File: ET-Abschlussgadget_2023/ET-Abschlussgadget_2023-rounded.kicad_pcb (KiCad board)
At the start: 2 copper layers, 85 x 54 mm, 35 parts, among them J1 PB0, J2 PB1, J3 UPDI / RESET, J4 EXTCLK, J5 EXTCLK, J6 EXTCLK, SW1 ON/OFF, U1 ATtiny414-SS

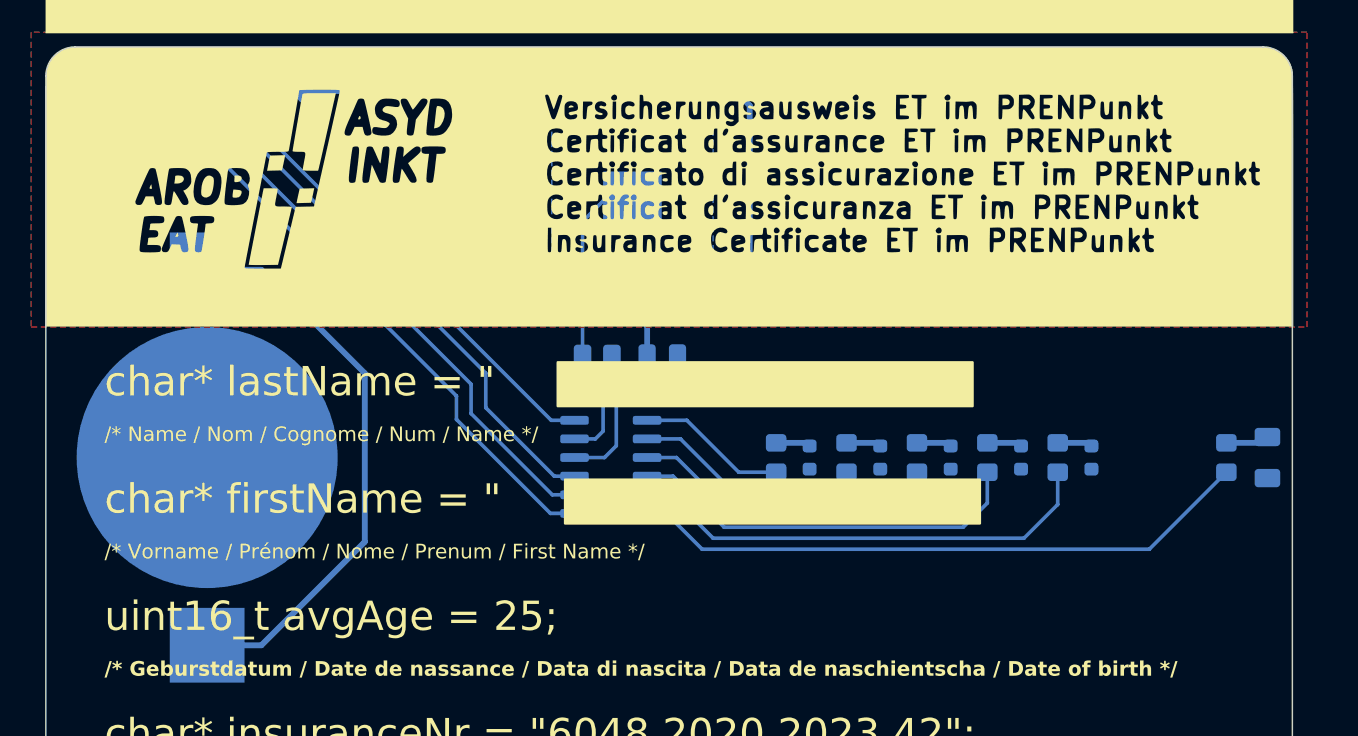
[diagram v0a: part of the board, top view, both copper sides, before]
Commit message: Redone whole layout based around new MCU, button and batteryholder-footprints are still placeholder tbd
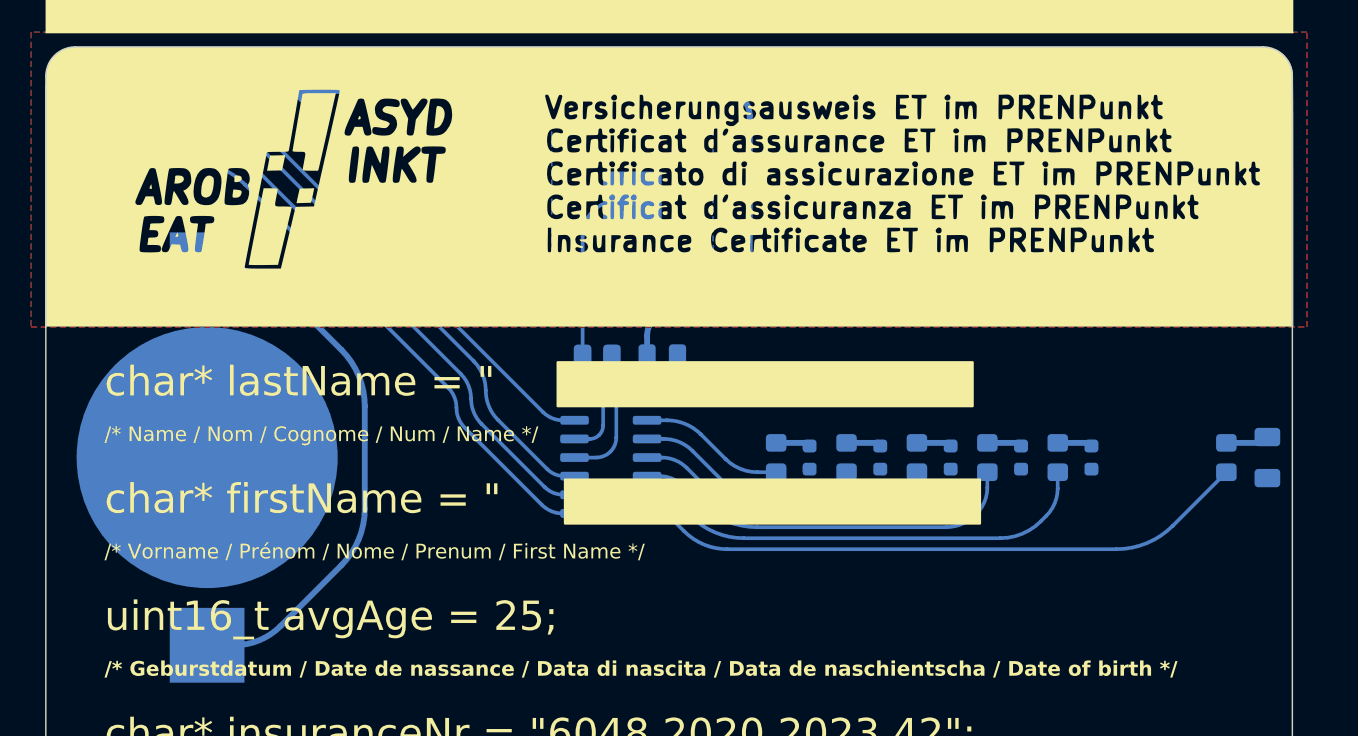
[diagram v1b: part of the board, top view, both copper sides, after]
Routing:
- net Net-(BT1-+): track 38.8 -> 37.9 mm
- net Net-(J2-Pin_1): track 47.0 -> 46.2 mm
- net Net-(J1-Pin_1): track 44.8 -> 44.0 mm
- net /LED 1: track 32.4 -> 31.7 mm
- net VCC: track 56.0 -> 55.3 mm
- net /LED 2: track 27.4 -> 26.8 mm
- net /LED 3: track 22.2 -> 21.6 mm
- net /UPDI / RESET: track 39.3 -> 38.8 mm
- net /LED 4: track 17.1 -> 16.6 mm
- net /LED IR: track 42.7 -> 42.1 mm

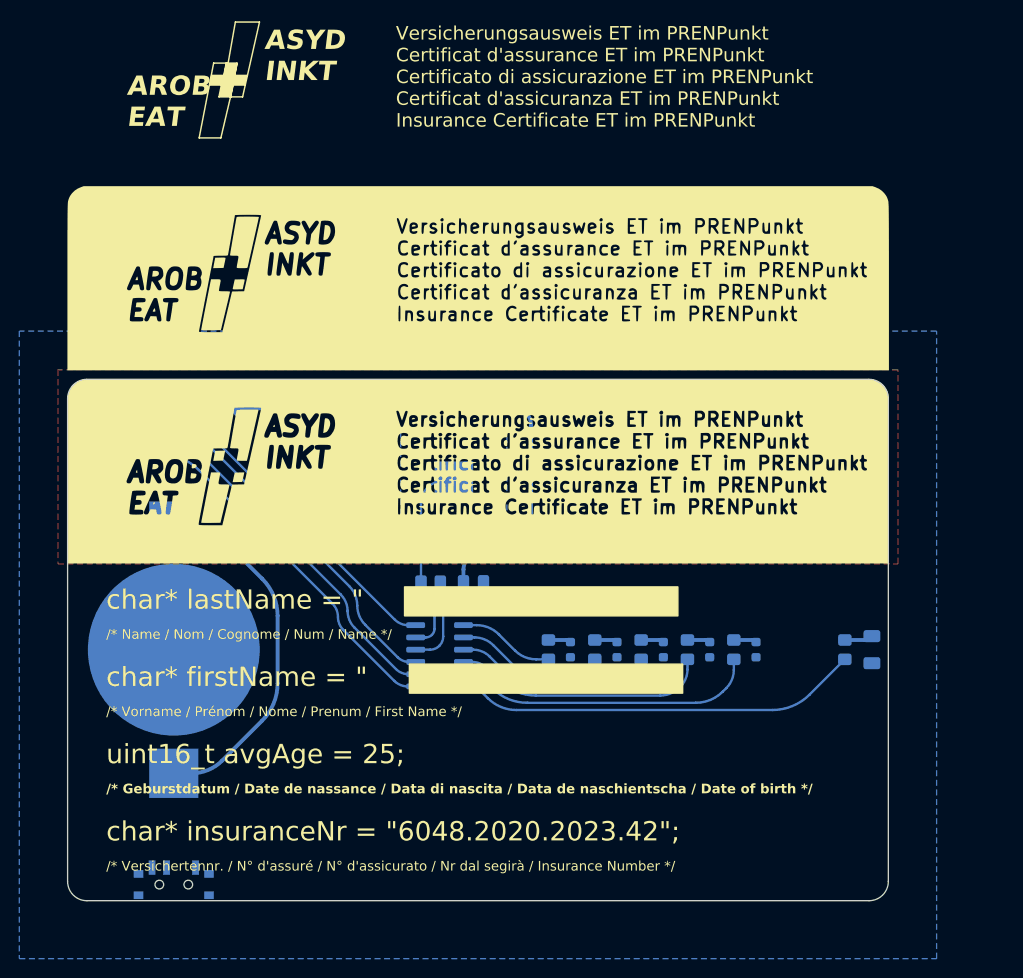
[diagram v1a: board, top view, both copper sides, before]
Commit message: Improve back silkscreen and routing
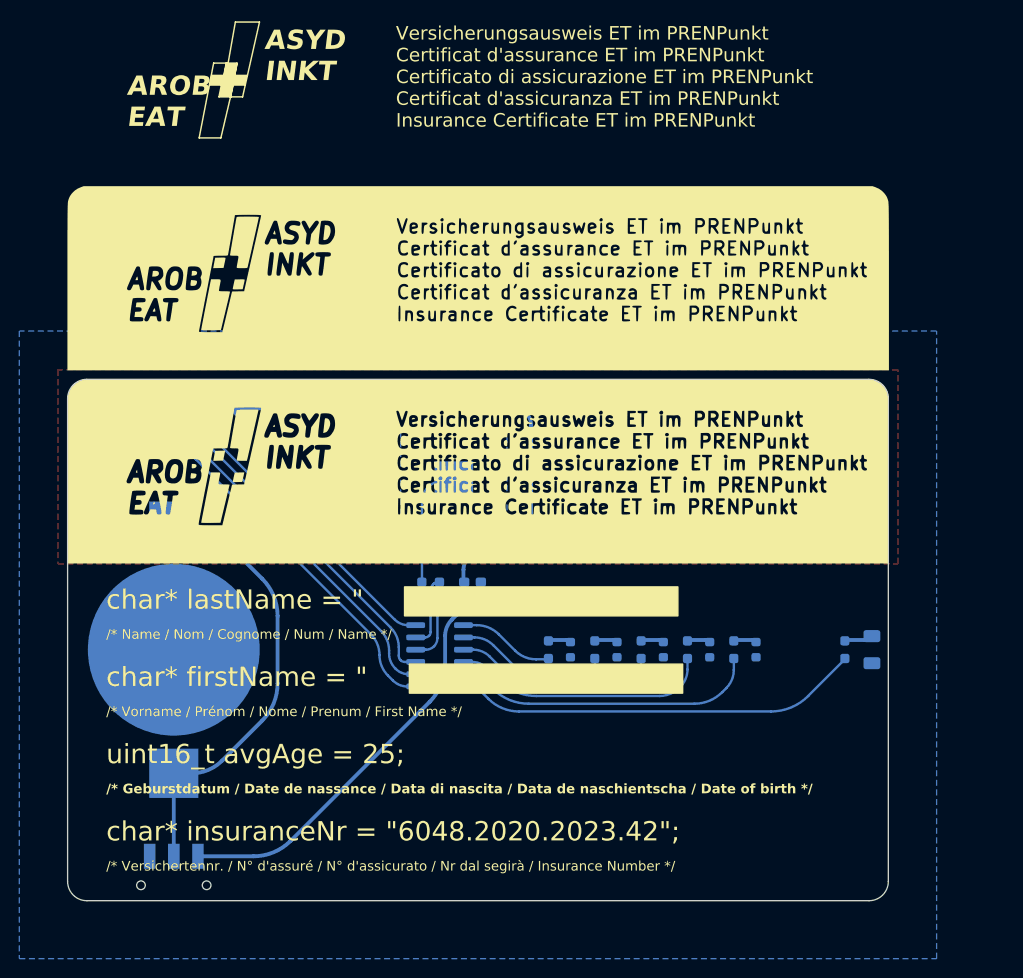
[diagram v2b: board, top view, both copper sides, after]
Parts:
- added kibuzzard-64480F6A: G***, kibuzzard-64480F6A, B.Cu at (128.7, 124.8)
- C1: footprint Capacitor_SMD:C_0805_2012Metric_Pad1.18x1.45mm_HandSolder -> Capacitor_SMD:C_0603_1608Metric_Pad1.08x0.95mm_HandSolder
- R1, R2, R3, R4, R5, R6, R7: footprint Resistor_SMD:R_0805_2012Metric_Pad1.20x1.40mm_HandSolder -> Resistor_SMD:R_0603_1608Metric_Pad0.98x0.95mm_HandSolder
- SW1: footprint Button_Switch_SMD:SW_SPDT_PCM12 -> Button_Switch_SMD:DEALON_MK-12D04-G2
- moved SW1 0.40 mm to (111.0, 132.4), turned to 0 degrees
- moved C1 0.10 mm to (141.9, 101.0)
- turned D1 to 90 degrees
- turned D2 to 90 degrees
- turned D3 to 90 degrees
- turned D4 to 90 degrees
- turned D5 to 90 degrees
- turned D6 to 90 degrees
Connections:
- D1 pad 1: Net-(D1-K) -> GND
- D1 pad 2: GND -> Net-(D1-A)
- D2 pad 1: Net-(D2-K) -> GND
- D2 pad 2: GND -> Net-(D2-A)
- D3 pad 1: Net-(D3-K) -> GND
- D3 pad 2: GND -> Net-(D3-A)
- D4 pad 1: Net-(D4-K) -> GND
- D4 pad 2: GND -> Net-(D4-A)
- D5 pad 1: Net-(D5-K) -> GND
- D5 pad 2: GND -> Net-(D5-A)
- D6 pad 1: Net-(D6-K) -> GND
- D6 pad 2: GND -> Net-(D6-A)
- R1 pad 1: Net-(D1-K) -> Net-(D1-A)
- R2 pad 1: Net-(D2-K) -> Net-(D2-A)
- R3 pad 2: Net-(D3-K) -> Net-(D3-A)
- R4 pad 2: Net-(D4-K) -> Net-(D4-A)
- R6 pad 1: Net-(D5-K) -> Net-(D5-A)
- R7 pad 1: Net-(D6-K) -> Net-(D6-A)
- SW1 pad 1: VCC -> unconnected-(SW1-A-Pad1)
- SW1 pad 3: unconnected-(SW1-C-Pad3) -> VCC
- U1 pad 12: /Cap_Pad -> /Cap_Pad / ADC1
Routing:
- net VCC: track 55.3 -> 96.1 mm
- net Net-(BT1-+): track 37.9 -> 47.1 mm
- net /Cap_Pad: track 20.5 -> 12.8 mm
- net /Cap_Pad / ADC1: track 9.35 -> 16.2 mm
- net Net-(D1-K): track 2.93 -> 0.00 mm
- net Net-(D1-A): track 0.00 -> 2.93 mm
- net Net-(D3-K): track 2.37 -> 0.00 mm
- net Net-(D3-A): track 0.00 -> 2.37 mm
- net Net-(D5-K): track 2.37 -> 0.00 mm
- net Net-(D5-A): track 0.00 -> 2.37 mm
- net Net-(D2-K): track 2.37 -> 0.00 mm
- net Net-(D2-A): track 0.00 -> 2.37 mm
- net Net-(D4-K): track 2.37 -> 0.00 mm
- net Net-(D4-A): track 0.00 -> 2.37 mm
- net Net-(D6-K): track 2.35 -> 0.00 mm
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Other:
- board text added: "ON"
- board text removed: "SCAN ME!"

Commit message: Move switch, Move testpads, Add spotify code
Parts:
- added G***: LOGO, LOGO, B.Cu at (127.5, 98.1)
- BT1: footprint Battery:BatteryHolder_Keystone_3002_1x2032 -> easyeda2kicad:BAT-SMD_CR2032-3V
- G*** (x2): value LOGO -> LOGO1
- SW1: footprint Button_Switch_SMD:DEALON_MK-12D04-G2 -> easyeda2kicad:SW-TH_MSK12C02
- moved SW1 8.86 mm to (103.9, 127.1), turned to 90 degrees
- moved J5 1.38 mm to (116.6, 83.0)
- moved J6 0.92 mm to (114.1, 83.0)
- moved J4 0.46 mm to (111.5, 83.0)
- moved J2 0.20 mm to (102.8, 83.0)
- turned BT1 to 180 degrees
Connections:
- SW1 pad 1: unconnected-(SW1-A-Pad1) -> VCC
- SW1 pad 3: VCC -> unconnected-(SW1-C-Pad3)
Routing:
- net VCC: track 96.1 -> 107.4 mm
- net Net-(BT1-+): track 47.1 -> 48.7 mm
- net /EXTCLK: track 33.3 -> 34.5 mm
- net Net-(J2-Pin_1): track 45.9 -> 46.9 mm
- net Net-(J1-Pin_1): track 43.5 -> 44.3 mm
- net /LED 1: track 31.8 -> 32.5 mm
- net /LED 2: track 26.8 -> 27.5 mm
- net /LED 3: track 21.6 -> 22.2 mm
- net /LED IR: track 42.3 -> 42.8 mm
- net /LED 4: track 16.6 -> 17.1 mm
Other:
- board text removed: "ET: {dblquote}Wie WI, nur besser{dblquote}"

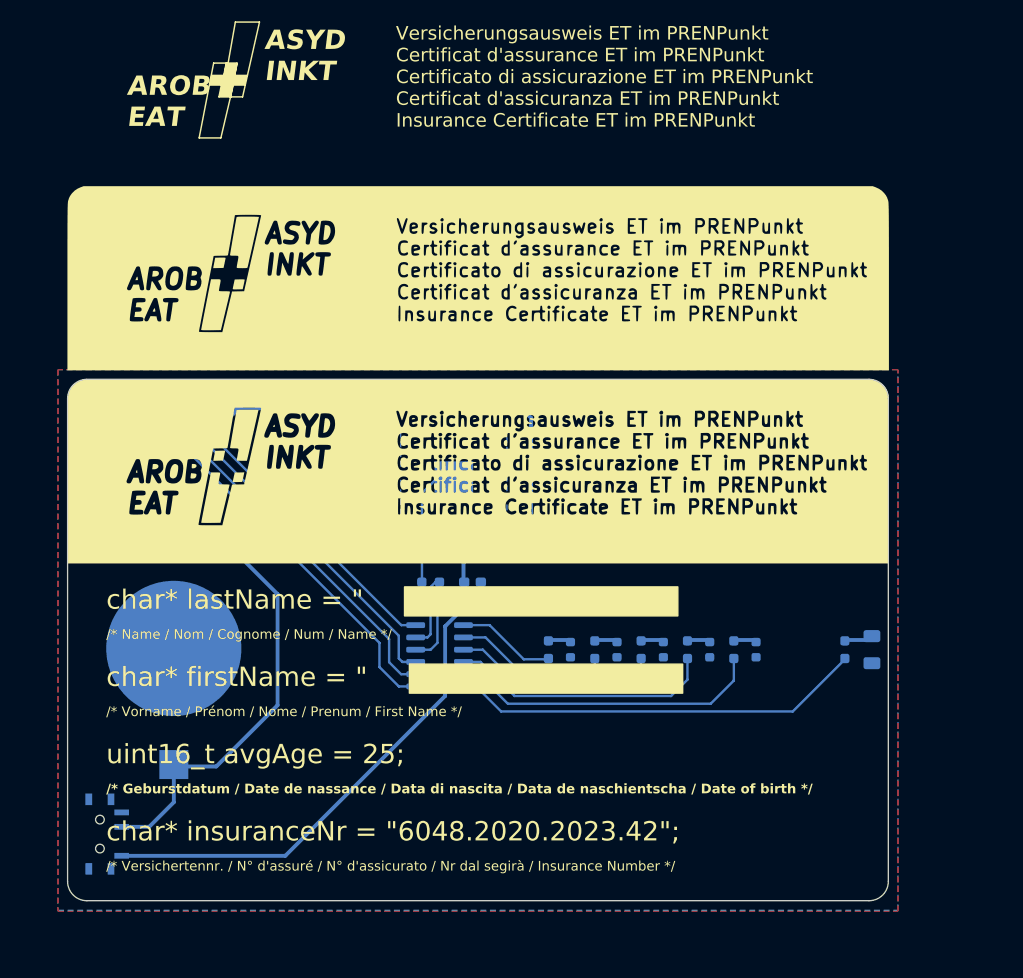
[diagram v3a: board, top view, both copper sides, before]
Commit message: Improve back copper pattern
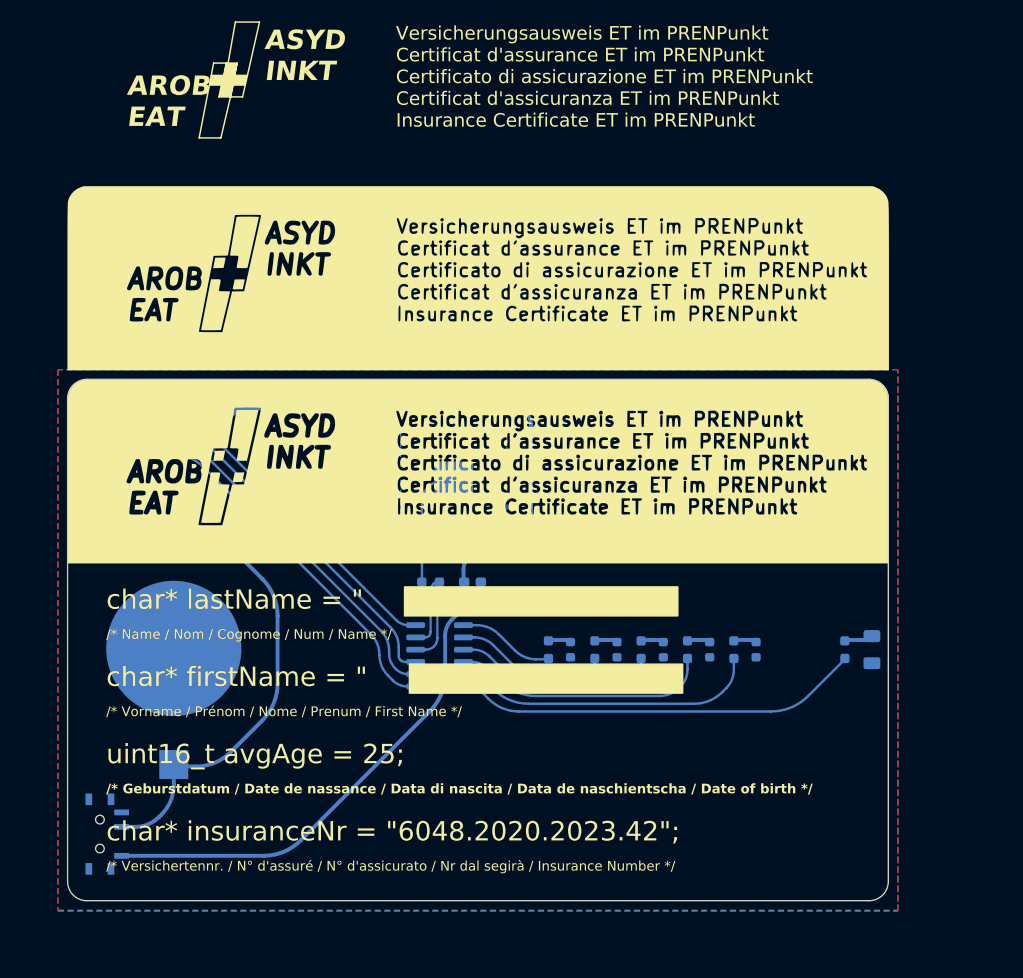
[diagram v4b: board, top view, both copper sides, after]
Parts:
- removed the G*** at (127.5, 98.1)
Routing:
- net Net-(BT1-+): track 48.7 -> 47.1 mm
- net VCC: track 107.4 -> 106.0 mm
- net Net-(J2-Pin_1): track 46.9 -> 46.0 mm
- net Net-(J1-Pin_1): track 44.3 -> 43.5 mm
- net /LED 1: track 32.5 -> 31.8 mm
- net /LED 2: track 27.5 -> 26.8 mm
- net /LED 3: track 22.2 -> 21.6 mm
- net /UPDI / RESET: track 40.0 -> 39.4 mm
- net /LED IR: track 42.8 -> 42.3 mm
- net /LED 4: track 17.1 -> 16.6 mm

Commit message: Fix spotify code
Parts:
- added G***: LOGO, LOGO, B.Cu at (127.9, 98.0)
